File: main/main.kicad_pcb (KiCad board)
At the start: 2 copper layers, 100 x 100 mm, 251 parts, among them J1 USB_C_Receptacle, J2 SWD, Q1 BSS138, SW1 SW_SPST, SW2 SW_SPST, SW3 SW_SPST, SW4 SW_SPST, SW5 SW_SPST, SW6 SW_SPST, U1 LN6206P332MR-G, U2 STM32F401CBUx, Y1 Crystal

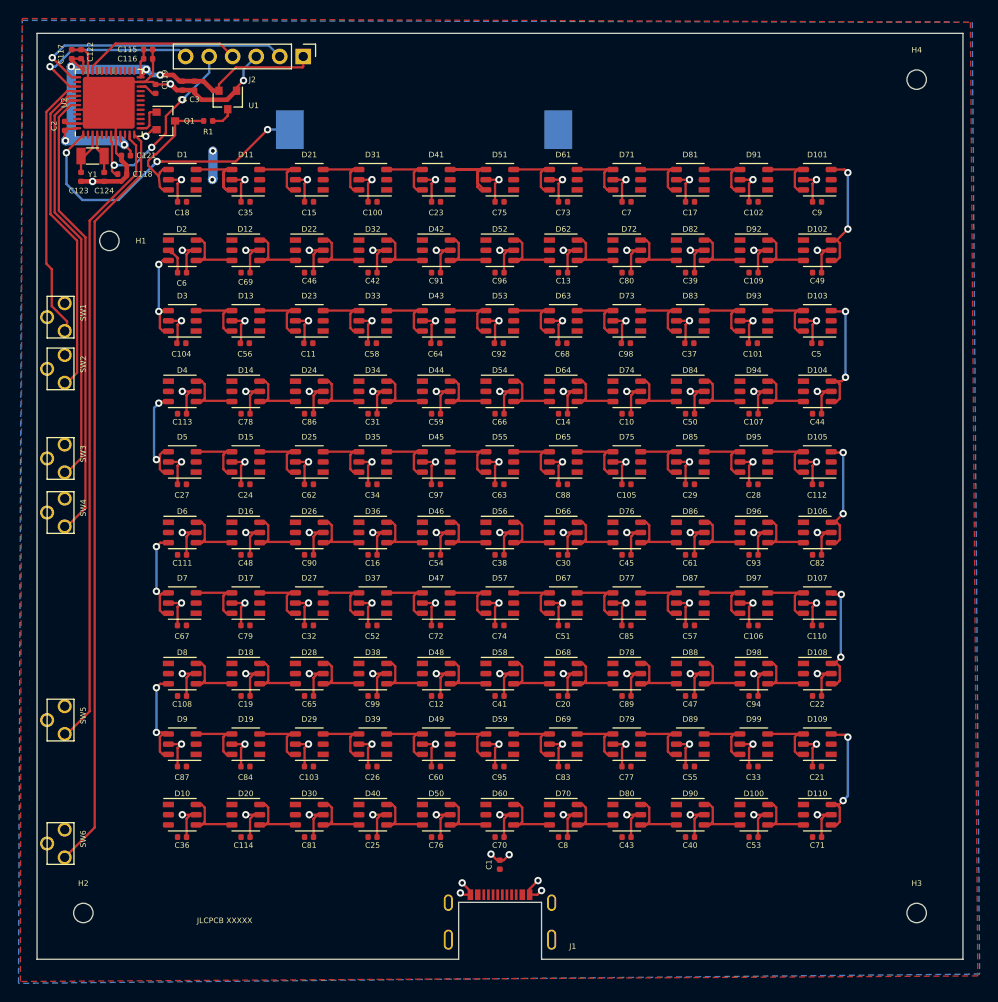
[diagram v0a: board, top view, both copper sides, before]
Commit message: made spacer layer, replaces Ws2813 with WS2812, fixed fabrication for v0.0.0, now v0.1.0
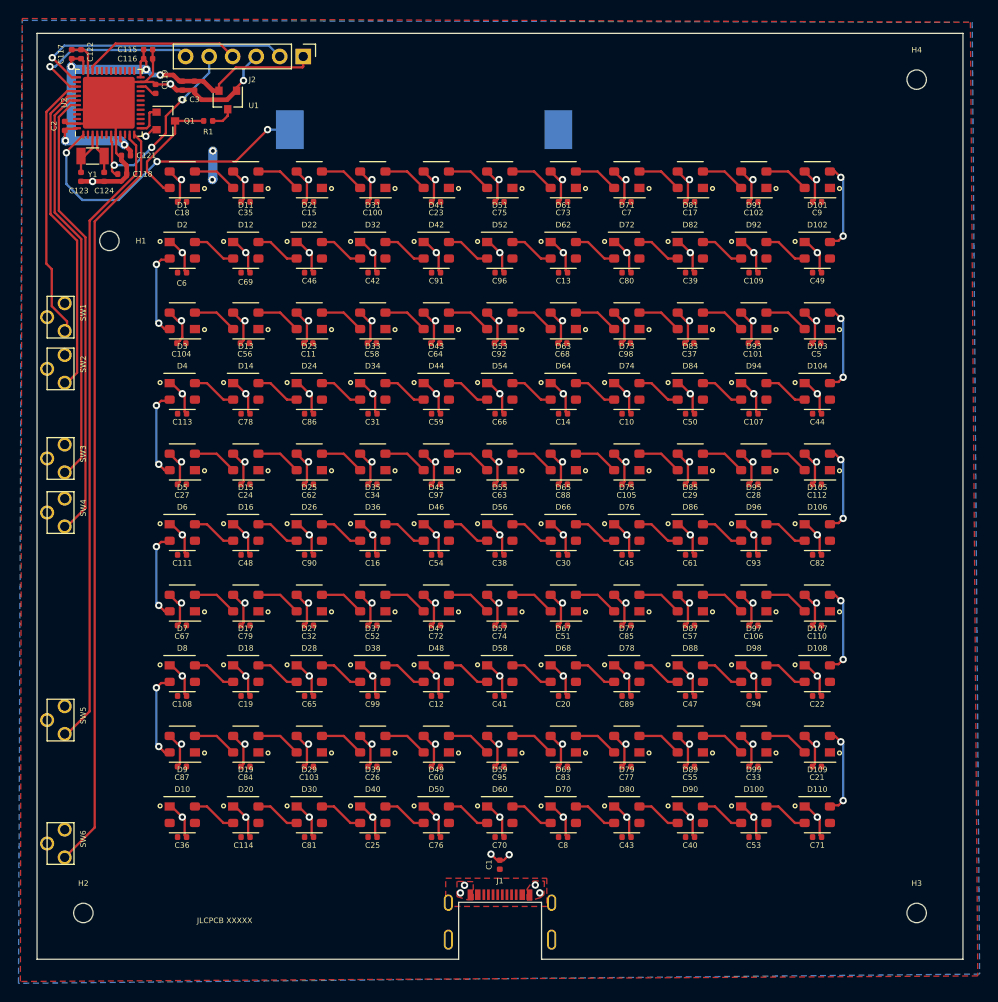
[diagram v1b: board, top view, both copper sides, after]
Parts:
- C118: value 10N -> 100N
- C119: value 2U2 -> 4U7
- C123, C124: value 21P -> 20P
- C4: value 10U -> 4U7
- D1, D10, D100, D101, D102, D103, D104, D105, D106, D107, D108, D109, D11, D110, D12, D13, D14, D15, D16, D17, D18, D19, D2, D20, D21, D22, D23, D24, D25, D26, D27, D28, D29, D3, D30, D31, D32, D33, D34, D35, D36, D37, D38, D39, D4, D40, D41, D42, D43, D44, D45, D46, D47, D48, D49, D5, D50, D51, D52, D53, D54, D55, D56, D57, D58, D59, D6, D60, D61, D62, D63, D64, D65, D66, D67, D68, D69, D7, D70, D71, D72, D73, D74, D75, D76, D77, D78, D79, D8, D80, D81, D82, D83, D84, D85, D86, D87, D88, D89, D9, D90, D91, D92, D93, D94, D95, D96, D97, D98, D99: value WS2813-Mini -> WS2812B-MINI; footprint william_led:WS2813-Mini-3.5mm_x_3.5mm -> william_led:WS2812B_v3-MINI
- J1: value USB_C_Receptacle -> USB_C_Receptacle_USB2.0
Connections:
- D1 pad 2: +5V -> Net-(D1-Pad2)
- D1 pad 3: Net-(D1-Pad3) -> GND
- D10 pad 1: +5V -> GND
- D10 pad 2: +5V -> /LEDs/DOUT
- D10 pad 3: (no net) -> +5V
- D100 pad 1: +5V -> GND
- D100 pad 2: +5V -> Net-(D100-Pad2)
- D100 pad 3: Net-(D100-Pad3) -> +5V
- D101 pad 2: +5V -> Net-(D101-Pad2)
- D101 pad 3: Net-(D101-Pad3) -> GND
- D102 pad 1: +5V -> GND
- D102 pad 2: +5V -> Net-(D102-Pad2)
- D102 pad 3: Net-(D102-Pad3) -> +5V
- D102 pad 4: Net-(D101-Pad3) -> Net-(D101-Pad2)
- D103 pad 2: +5V -> Net-(D103-Pad2)
- D103 pad 3: Net-(D103-Pad3) -> GND
- D104 pad 1: +5V -> GND
- D104 pad 2: +5V -> Net-(D104-Pad2)
- D104 pad 3: Net-(D104-Pad3) -> +5V
- D104 pad 4: Net-(D103-Pad3) -> Net-(D103-Pad2)
- D105 pad 2: +5V -> Net-(D105-Pad2)
- D105 pad 3: Net-(D105-Pad3) -> GND
- D106 pad 1: +5V -> GND
- D106 pad 2: +5V -> Net-(D106-Pad2)
- D106 pad 3: Net-(D106-Pad3) -> +5V
- D106 pad 4: Net-(D105-Pad3) -> Net-(D105-Pad2)
- D107 pad 2: +5V -> Net-(D107-Pad2)
- D107 pad 3: Net-(D107-Pad3) -> GND
- D108 pad 1: +5V -> GND
- D108 pad 2: +5V -> Net-(D108-Pad2)
- D108 pad 3: Net-(D108-Pad3) -> +5V
- D108 pad 4: Net-(D107-Pad3) -> Net-(D107-Pad2)
- D109 pad 2: +5V -> Net-(D109-Pad2)
- D109 pad 3: Net-(D109-Pad3) -> GND
- D11 pad 2: +5V -> Net-(D11-Pad2)
- D11 pad 3: Net-(D11-Pad3) -> GND
- D11 pad 4: Net-(D1-Pad3) -> Net-(D1-Pad2)
- D110 pad 1: +5V -> GND
- D110 pad 2: +5V -> Net-(D100-Pad4)
- D110 pad 3: Net-(D100-Pad4) -> +5V
- D110 pad 4: Net-(D109-Pad3) -> Net-(D109-Pad2)
- D12 pad 1: +5V -> GND
- D12 pad 2: +5V -> Net-(D12-Pad2)
- D12 pad 3: Net-(D12-Pad3) -> +5V
- D13 pad 2: +5V -> Net-(D13-Pad2)
- D13 pad 3: Net-(D13-Pad3) -> GND
- D14 pad 1: +5V -> GND
- D14 pad 2: +5V -> Net-(D14-Pad2)
- D14 pad 3: Net-(D14-Pad3) -> +5V
- D15 pad 2: +5V -> Net-(D15-Pad2)
- D15 pad 3: Net-(D15-Pad3) -> GND
- D16 pad 1: +5V -> GND
- D16 pad 2: +5V -> Net-(D16-Pad2)
- D16 pad 3: Net-(D16-Pad3) -> +5V
- D17 pad 2: +5V -> Net-(D17-Pad2)
- D17 pad 3: Net-(D17-Pad3) -> GND
- D18 pad 1: +5V -> GND
- D18 pad 2: +5V -> Net-(D18-Pad2)
- D18 pad 3: Net-(D18-Pad3) -> +5V
- D19 pad 2: +5V -> Net-(D19-Pad2)
- D19 pad 3: Net-(D19-Pad3) -> GND
- D2 pad 1: +5V -> GND
- D2 pad 2: +5V -> Net-(D2-Pad2)
- D2 pad 3: Net-(D2-Pad3) -> +5V
- D2 pad 4: Net-(D12-Pad3) -> Net-(D12-Pad2)
- D20 pad 1: +5V -> GND
- D20 pad 2: +5V -> Net-(D10-Pad4)
- D20 pad 3: Net-(D10-Pad4) -> +5V
- D21 pad 2: +5V -> Net-(D21-Pad2)
- D21 pad 3: Net-(D21-Pad3) -> GND
- D21 pad 4: Net-(D11-Pad3) -> Net-(D11-Pad2)
- D22 pad 1: +5V -> GND
- D22 pad 2: +5V -> Net-(D12-Pad4)
- D22 pad 3: Net-(D12-Pad4) -> +5V
- D23 pad 2: +5V -> Net-(D23-Pad2)
- D23 pad 3: Net-(D23-Pad3) -> GND
- D23 pad 4: Net-(D13-Pad3) -> Net-(D13-Pad2)
- D24 pad 1: +5V -> GND
- D24 pad 2: +5V -> Net-(D14-Pad4)
- D24 pad 3: Net-(D14-Pad4) -> +5V
- D25 pad 2: +5V -> Net-(D25-Pad2)
- D25 pad 3: Net-(D25-Pad3) -> GND
- D25 pad 4: Net-(D15-Pad3) -> Net-(D15-Pad2)
- D26 pad 1: +5V -> GND
- D26 pad 2: +5V -> Net-(D16-Pad4)
- D26 pad 3: Net-(D16-Pad4) -> +5V
- D27 pad 2: +5V -> Net-(D27-Pad2)
- D27 pad 3: Net-(D27-Pad3) -> GND
- D27 pad 4: Net-(D17-Pad3) -> Net-(D17-Pad2)
- D28 pad 1: +5V -> GND
- D28 pad 2: +5V -> Net-(D18-Pad4)
- D28 pad 3: Net-(D18-Pad4) -> +5V
- D29 pad 2: +5V -> Net-(D29-Pad2)
- D29 pad 3: Net-(D29-Pad3) -> GND
- D29 pad 4: Net-(D19-Pad3) -> Net-(D19-Pad2)
- D3 pad 2: +5V -> Net-(D13-Pad4)
- D3 pad 3: Net-(D13-Pad4) -> GND
- D3 pad 4: Net-(D2-Pad3) -> Net-(D2-Pad2)
- D30 pad 1: +5V -> GND
- D30 pad 2: +5V -> Net-(D20-Pad4)
- D30 pad 3: Net-(D20-Pad4) -> +5V
- D31 pad 2: +5V -> Net-(D31-Pad2)
- D31 pad 3: Net-(D31-Pad3) -> GND
- D31 pad 4: Net-(D21-Pad3) -> Net-(D21-Pad2)
- D32 pad 1: +5V -> GND
- D32 pad 2: +5V -> Net-(D22-Pad4)
- D32 pad 3: Net-(D22-Pad4) -> +5V
- D33 pad 2: +5V -> Net-(D33-Pad2)
- D33 pad 3: Net-(D33-Pad3) -> GND
- D33 pad 4: Net-(D23-Pad3) -> Net-(D23-Pad2)
- D34 pad 1: +5V -> GND
- D34 pad 2: +5V -> Net-(D24-Pad4)
- D34 pad 3: Net-(D24-Pad4) -> +5V
- D35 pad 2: +5V -> Net-(D35-Pad2)
- D35 pad 3: Net-(D35-Pad3) -> GND
- D35 pad 4: Net-(D25-Pad3) -> Net-(D25-Pad2)
- D36 pad 1: +5V -> GND
- D36 pad 2: +5V -> Net-(D26-Pad4)
- D36 pad 3: Net-(D26-Pad4) -> +5V
- D37 pad 2: +5V -> Net-(D37-Pad2)
- D37 pad 3: Net-(D37-Pad3) -> GND
- D37 pad 4: Net-(D27-Pad3) -> Net-(D27-Pad2)
- D38 pad 1: +5V -> GND
- D38 pad 2: +5V -> Net-(D28-Pad4)
- D38 pad 3: Net-(D28-Pad4) -> +5V
- D39 pad 2: +5V -> Net-(D39-Pad2)
- D39 pad 3: Net-(D39-Pad3) -> GND
- D39 pad 4: Net-(D29-Pad3) -> Net-(D29-Pad2)
- D4 pad 1: +5V -> GND
- D4 pad 2: +5V -> Net-(D4-Pad2)
- D4 pad 3: Net-(D4-Pad3) -> +5V
- D4 pad 4: Net-(D14-Pad3) -> Net-(D14-Pad2)
- D40 pad 1: +5V -> GND
- D40 pad 2: +5V -> Net-(D30-Pad4)
- D40 pad 3: Net-(D30-Pad4) -> +5V
- D41 pad 2: +5V -> Net-(D41-Pad2)
- D41 pad 3: Net-(D41-Pad3) -> GND
- D41 pad 4: Net-(D31-Pad3) -> Net-(D31-Pad2)
- D42 pad 1: +5V -> GND
- D42 pad 2: +5V -> Net-(D32-Pad4)
- D42 pad 3: Net-(D32-Pad4) -> +5V
- D43 pad 2: +5V -> Net-(D43-Pad2)
- D43 pad 3: Net-(D43-Pad3) -> GND
- D43 pad 4: Net-(D33-Pad3) -> Net-(D33-Pad2)
- D44 pad 1: +5V -> GND
- D44 pad 2: +5V -> Net-(D34-Pad4)
- D44 pad 3: Net-(D34-Pad4) -> +5V
- D45 pad 2: +5V -> Net-(D45-Pad2)
- D45 pad 3: Net-(D45-Pad3) -> GND
- D45 pad 4: Net-(D35-Pad3) -> Net-(D35-Pad2)
- D46 pad 1: +5V -> GND
- D46 pad 2: +5V -> Net-(D36-Pad4)
- D46 pad 3: Net-(D36-Pad4) -> +5V
- D47 pad 2: +5V -> Net-(D47-Pad2)
- D47 pad 3: Net-(D47-Pad3) -> GND
- D47 pad 4: Net-(D37-Pad3) -> Net-(D37-Pad2)
- D48 pad 1: +5V -> GND
- D48 pad 2: +5V -> Net-(D38-Pad4)
- D48 pad 3: Net-(D38-Pad4) -> +5V
- D49 pad 2: +5V -> Net-(D49-Pad2)
- D49 pad 3: Net-(D49-Pad3) -> GND
- D49 pad 4: Net-(D39-Pad3) -> Net-(D39-Pad2)
- D5 pad 2: +5V -> Net-(D15-Pad4)
- D5 pad 3: Net-(D15-Pad4) -> GND
- D5 pad 4: Net-(D4-Pad3) -> Net-(D4-Pad2)
- D50 pad 1: +5V -> GND
- D50 pad 2: +5V -> Net-(D40-Pad4)
- D50 pad 3: Net-(D40-Pad4) -> +5V
- D51 pad 2: +5V -> Net-(D51-Pad2)
- D51 pad 3: Net-(D51-Pad3) -> GND
- D51 pad 4: Net-(D41-Pad3) -> Net-(D41-Pad2)
- D52 pad 1: +5V -> GND
- D52 pad 2: +5V -> Net-(D42-Pad4)
- D52 pad 3: Net-(D42-Pad4) -> +5V
- D53 pad 2: +5V -> Net-(D53-Pad2)
- D53 pad 3: Net-(D53-Pad3) -> GND
- D53 pad 4: Net-(D43-Pad3) -> Net-(D43-Pad2)
- D54 pad 1: +5V -> GND
- D54 pad 2: +5V -> Net-(D44-Pad4)
- D54 pad 3: Net-(D44-Pad4) -> +5V
- D55 pad 2: +5V -> Net-(D55-Pad2)
- D55 pad 3: Net-(D55-Pad3) -> GND
- D55 pad 4: Net-(D45-Pad3) -> Net-(D45-Pad2)
- D56 pad 1: +5V -> GND
- D56 pad 2: +5V -> Net-(D46-Pad4)
- D56 pad 3: Net-(D46-Pad4) -> +5V
- D57 pad 2: +5V -> Net-(D57-Pad2)
- D57 pad 3: Net-(D57-Pad3) -> GND
- D57 pad 4: Net-(D47-Pad3) -> Net-(D47-Pad2)
- D58 pad 1: +5V -> GND
- D58 pad 2: +5V -> Net-(D48-Pad4)
- D58 pad 3: Net-(D48-Pad4) -> +5V
- D59 pad 2: +5V -> Net-(D59-Pad2)
- D59 pad 3: Net-(D59-Pad3) -> GND
- D59 pad 4: Net-(D49-Pad3) -> Net-(D49-Pad2)
- D6 pad 1: +5V -> GND
- D6 pad 2: +5V -> Net-(D6-Pad2)
- D6 pad 3: Net-(D6-Pad3) -> +5V
- D6 pad 4: Net-(D16-Pad3) -> Net-(D16-Pad2)
- D60 pad 1: +5V -> GND
- D60 pad 2: +5V -> Net-(D50-Pad4)
- D60 pad 3: Net-(D50-Pad4) -> +5V
- D61 pad 2: +5V -> Net-(D61-Pad2)
- D61 pad 3: Net-(D61-Pad3) -> GND
- D61 pad 4: Net-(D51-Pad3) -> Net-(D51-Pad2)
- D62 pad 1: +5V -> GND
- D62 pad 2: +5V -> Net-(D52-Pad4)
- D62 pad 3: Net-(D52-Pad4) -> +5V
- D63 pad 2: +5V -> Net-(D63-Pad2)
- D63 pad 3: Net-(D63-Pad3) -> GND
- D63 pad 4: Net-(D53-Pad3) -> Net-(D53-Pad2)
- D64 pad 1: +5V -> GND
- D64 pad 2: +5V -> Net-(D54-Pad4)
- D64 pad 3: Net-(D54-Pad4) -> +5V
- D65 pad 2: +5V -> Net-(D65-Pad2)
- D65 pad 3: Net-(D65-Pad3) -> GND
- D65 pad 4: Net-(D55-Pad3) -> Net-(D55-Pad2)
- D66 pad 1: +5V -> GND
- D66 pad 2: +5V -> Net-(D56-Pad4)
- D66 pad 3: Net-(D56-Pad4) -> +5V
- D67 pad 2: +5V -> Net-(D67-Pad2)
- D67 pad 3: Net-(D67-Pad3) -> GND
- D67 pad 4: Net-(D57-Pad3) -> Net-(D57-Pad2)
- D68 pad 1: +5V -> GND
- D68 pad 2: +5V -> Net-(D58-Pad4)
- D68 pad 3: Net-(D58-Pad4) -> +5V
- D69 pad 2: +5V -> Net-(D69-Pad2)
- D69 pad 3: Net-(D69-Pad3) -> GND
- D69 pad 4: Net-(D59-Pad3) -> Net-(D59-Pad2)
- D7 pad 2: +5V -> Net-(D17-Pad4)
- D7 pad 3: Net-(D17-Pad4) -> GND
- D7 pad 4: Net-(D6-Pad3) -> Net-(D6-Pad2)
- D70 pad 1: +5V -> GND
- D70 pad 2: +5V -> Net-(D60-Pad4)
- D70 pad 3: Net-(D60-Pad4) -> +5V
- D71 pad 2: +5V -> Net-(D71-Pad2)
- D71 pad 3: Net-(D71-Pad3) -> GND
- D71 pad 4: Net-(D61-Pad3) -> Net-(D61-Pad2)
- D72 pad 1: +5V -> GND
- D72 pad 2: +5V -> Net-(D62-Pad4)
- D72 pad 3: Net-(D62-Pad4) -> +5V
- D73 pad 2: +5V -> Net-(D73-Pad2)
- D73 pad 3: Net-(D73-Pad3) -> GND
- D73 pad 4: Net-(D63-Pad3) -> Net-(D63-Pad2)
- D74 pad 1: +5V -> GND
- D74 pad 2: +5V -> Net-(D64-Pad4)
- D74 pad 3: Net-(D64-Pad4) -> +5V
- D75 pad 2: +5V -> Net-(D75-Pad2)
- D75 pad 3: Net-(D75-Pad3) -> GND
- D75 pad 4: Net-(D65-Pad3) -> Net-(D65-Pad2)
- D76 pad 1: +5V -> GND
- D76 pad 2: +5V -> Net-(D66-Pad4)
- D76 pad 3: Net-(D66-Pad4) -> +5V
- D77 pad 2: +5V -> Net-(D77-Pad2)
- D77 pad 3: Net-(D77-Pad3) -> GND
- D77 pad 4: Net-(D67-Pad3) -> Net-(D67-Pad2)
- D78 pad 1: +5V -> GND
- D78 pad 2: +5V -> Net-(D68-Pad4)
- D78 pad 3: Net-(D68-Pad4) -> +5V
- D79 pad 2: +5V -> Net-(D79-Pad2)
- D79 pad 3: Net-(D79-Pad3) -> GND
- D79 pad 4: Net-(D69-Pad3) -> Net-(D69-Pad2)
- D8 pad 1: +5V -> GND
- D8 pad 2: +5V -> Net-(D8-Pad2)
- D8 pad 3: Net-(D8-Pad3) -> +5V
- D8 pad 4: Net-(D18-Pad3) -> Net-(D18-Pad2)
- D80 pad 1: +5V -> GND
- D80 pad 2: +5V -> Net-(D70-Pad4)
- D80 pad 3: Net-(D70-Pad4) -> +5V
- D81 pad 2: +5V -> Net-(D81-Pad2)
- D81 pad 3: Net-(D81-Pad3) -> GND
- D81 pad 4: Net-(D71-Pad3) -> Net-(D71-Pad2)
- D82 pad 1: +5V -> GND
- D82 pad 2: +5V -> Net-(D72-Pad4)
- D82 pad 3: Net-(D72-Pad4) -> +5V
- D83 pad 2: +5V -> Net-(D83-Pad2)
- D83 pad 3: Net-(D83-Pad3) -> GND
- D83 pad 4: Net-(D73-Pad3) -> Net-(D73-Pad2)
- D84 pad 1: +5V -> GND
- D84 pad 2: +5V -> Net-(D74-Pad4)
- D84 pad 3: Net-(D74-Pad4) -> +5V
- D85 pad 2: +5V -> Net-(D85-Pad2)
- D85 pad 3: Net-(D85-Pad3) -> GND
- D85 pad 4: Net-(D75-Pad3) -> Net-(D75-Pad2)
- D86 pad 1: +5V -> GND
- D86 pad 2: +5V -> Net-(D76-Pad4)
- D86 pad 3: Net-(D76-Pad4) -> +5V
- D87 pad 2: +5V -> Net-(D87-Pad2)
- D87 pad 3: Net-(D87-Pad3) -> GND
- D87 pad 4: Net-(D77-Pad3) -> Net-(D77-Pad2)
- D88 pad 1: +5V -> GND
- D88 pad 2: +5V -> Net-(D78-Pad4)
- D88 pad 3: Net-(D78-Pad4) -> +5V
- D89 pad 2: +5V -> Net-(D89-Pad2)
- D89 pad 3: Net-(D89-Pad3) -> GND
- D89 pad 4: Net-(D79-Pad3) -> Net-(D79-Pad2)
- D9 pad 2: +5V -> Net-(D19-Pad4)
- D9 pad 3: Net-(D19-Pad4) -> GND
- D9 pad 4: Net-(D8-Pad3) -> Net-(D8-Pad2)
- D90 pad 1: +5V -> GND
- D90 pad 2: +5V -> Net-(D80-Pad4)
- D90 pad 3: Net-(D80-Pad4) -> +5V
- D90 pad 4: Net-(D100-Pad3) -> Net-(D100-Pad2)
- D91 pad 2: +5V -> Net-(D101-Pad4)
- D91 pad 3: Net-(D101-Pad4) -> GND
- D91 pad 4: Net-(D81-Pad3) -> Net-(D81-Pad2)
- D92 pad 1: +5V -> GND
- D92 pad 2: +5V -> Net-(D82-Pad4)
- D92 pad 3: Net-(D82-Pad4) -> +5V
- D92 pad 4: Net-(D102-Pad3) -> Net-(D102-Pad2)
- D93 pad 2: +5V -> Net-(D103-Pad4)
- D93 pad 3: Net-(D103-Pad4) -> GND
- D93 pad 4: Net-(D83-Pad3) -> Net-(D83-Pad2)
- D94 pad 1: +5V -> GND
- D94 pad 2: +5V -> Net-(D84-Pad4)
- D94 pad 3: Net-(D84-Pad4) -> +5V
- D94 pad 4: Net-(D104-Pad3) -> Net-(D104-Pad2)
- D95 pad 2: +5V -> Net-(D105-Pad4)
- D95 pad 3: Net-(D105-Pad4) -> GND
- D95 pad 4: Net-(D85-Pad3) -> Net-(D85-Pad2)
- D96 pad 1: +5V -> GND
- D96 pad 2: +5V -> Net-(D86-Pad4)
- D96 pad 3: Net-(D86-Pad4) -> +5V
- D96 pad 4: Net-(D106-Pad3) -> Net-(D106-Pad2)
- D97 pad 2: +5V -> Net-(D107-Pad4)
- D97 pad 3: Net-(D107-Pad4) -> GND
- D97 pad 4: Net-(D87-Pad3) -> Net-(D87-Pad2)
- D98 pad 1: +5V -> GND
- D98 pad 2: +5V -> Net-(D88-Pad4)
- D98 pad 3: Net-(D88-Pad4) -> +5V
- D98 pad 4: Net-(D108-Pad3) -> Net-(D108-Pad2)
- D99 pad 2: +5V -> Net-(D109-Pad4)
- D99 pad 3: Net-(D109-Pad4) -> GND
- D99 pad 4: Net-(D89-Pad3) -> Net-(D89-Pad2)
- J1 pad A5: (no net) -> Net-(J1-PadA5)
- J1 pad A6: (no net) -> Net-(J1-PadA6)
- J1 pad A7: (no net) -> Net-(J1-PadA7)
- J1 pad A8: (no net) -> Net-(J1-PadA8)
- J1 pad B5: (no net) -> Net-(J1-PadB5)
- J1 pad B6: (no net) -> Net-(J1-PadB6)
- J1 pad B7: (no net) -> Net-(J1-PadB7)
- J1 pad B8: (no net) -> Net-(J1-PadB8)
- U2 pad 10: (no net) -> Net-(U2-Pad10)
- U2 pad 14: (no net) -> Net-(U2-Pad14)
- U2 pad 15: (no net) -> Net-(U2-Pad15)
- U2 pad 16: (no net) -> Net-(U2-Pad16)
- U2 pad 17: (no net) -> Net-(U2-Pad17)
- U2 pad 18: (no net) -> Net-(U2-Pad18)
- U2 pad 19: (no net) -> Net-(U2-Pad19)
- U2 pad 2: (no net) -> Net-(U2-Pad2)
- U2 pad 20: (no net) -> Net-(U2-Pad20)
- U2 pad 21: (no net) -> Net-(U2-Pad21)
- U2 pad 25: (no net) -> Net-(U2-Pad25)
- U2 pad 26: (no net) -> Net-(U2-Pad26)
- U2 pad 27: (no net) -> Net-(U2-Pad27)
- U2 pad 28: (no net) -> Net-(U2-Pad28)
- U2 pad 29: (no net) -> Net-(U2-Pad29)
- U2 pad 30: (no net) -> Net-(U2-Pad30)
- U2 pad 31: (no net) -> Net-(U2-Pad31)
- U2 pad 32: (no net) -> Net-(U2-Pad32)
- U2 pad 33: (no net) -> Net-(U2-Pad33)
- U2 pad 38: (no net) -> Net-(U2-Pad38)
- U2 pad 45: (no net) -> Net-(U2-Pad45)
- U2 pad 46: (no net) -> Net-(U2-Pad46)
- U2 pad 5: (no net) -> Net-(U2-Pad5)
- U2 pad 6: (no net) -> Net-(U2-Pad6)
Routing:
- net GND: track 544.6 -> 523.4 mm
- net Net-(D41-Pad3): track 14.8 -> 0.00 mm
- net Net-(D109-Pad3): track 14.1 -> 0.00 mm, vias 2 -> 0
- net Net-(D103-Pad3): track 14.1 -> 0.00 mm, vias 2 -> 0
- net Net-(D101-Pad3): track 13.4 -> 0.00 mm, vias 2 -> 0
- net Net-(D105-Pad3): track 13.3 -> 0.00 mm, vias 2 -> 0
- net Net-(D107-Pad3): track 13.0 -> 0.00 mm, vias 2 -> 0
- net Net-(D4-Pad3): track 11.6 -> 0.00 mm, vias 2 -> 0
- net Net-(D6-Pad3): track 11.4 -> 0.00 mm, vias 2 -> 0
- net Net-(D8-Pad3): track 11.3 -> 0.00 mm, vias 2 -> 0
- net Net-(D1-Pad3): track 11.2 -> 0.00 mm
- net Net-(D2-Pad3): track 11.0 -> 0.00 mm, vias 2 -> 0
- net Net-(D109-Pad2): track 0.00 -> 9.59 mm, vias 0 -> 2
- net Net-(D107-Pad2): track 0.00 -> 9.59 mm, vias 0 -> 2
- net Net-(D105-Pad2): track 0.00 -> 9.59 mm, vias 0 -> 2
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- added copper zone on F.Cu, net GND
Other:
- board text added: "WORD CLOCK v0.1.0 batch 0 12/11/2019"
- board text removed: "WORD CLOCK v0.0.0 batch 0 12/11/2019"

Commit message: added 4 more leds for minute-specific indicator
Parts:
- added C120: 100N, Capacitor_SMD:C_0402_1005Metric, F.Cu at (19.2, 96.0)
- added C125: 100N, Capacitor_SMD:C_0402_1005Metric, F.Cu at (31.4, 96.2)
- added C126: 100N, Capacitor_SMD:C_0402_1005Metric, F.Cu at (68.8, 97.0)
- added C127: 100N, Capacitor_SMD:C_0402_1005Metric, F.Cu at (81.1, 96.3)
- added D111: WS2812B-MINI, william_led:WS2812B_v3-MINI, F.Cu at (18.9, 92.4)
- added D112: WS2812B-MINI, william_led:WS2812B_v3-MINI, F.Cu at (31.2, 92.4)
- added D113: WS2812B-MINI, william_led:WS2812B_v3-MINI, F.Cu at (68.8, 92.4)
- added D114: WS2812B-MINI, william_led:WS2812B_v3-MINI, F.Cu at (81.1, 92.4)
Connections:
- D10 pad 2: /LEDs/DOUT -> Net-(D10-Pad2)
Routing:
- net Net-(D112-Pad2): track 0.00 -> 37.9 mm, vias 0 -> 6
- net GND: track 523.4 -> 542.2 mm, vias 120 -> 124
- net Net-(D10-Pad2): track 0.00 -> 11.7 mm, vias 0 -> 2
- net Net-(D113-Pad2): track 0.00 -> 10.3 mm, vias 0 -> 2
- net Net-(D111-Pad2): track 0.00 -> 10.2 mm, vias 0 -> 2

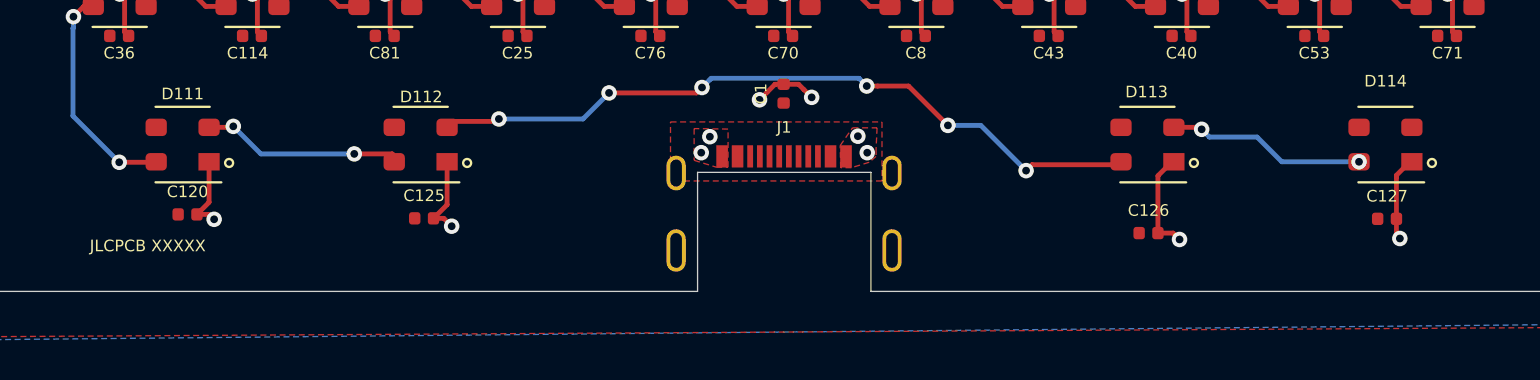
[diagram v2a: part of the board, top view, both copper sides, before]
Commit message: moved caps in to LEDs so they'd fit under hole
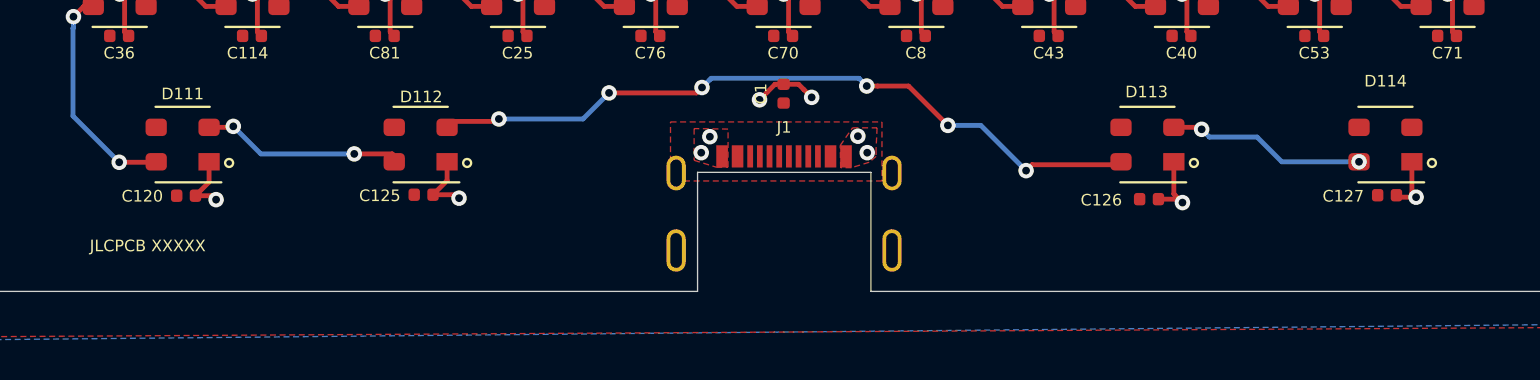
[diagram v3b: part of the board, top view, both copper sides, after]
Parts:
- moved C126 1.75 mm to (68.9, 95.2)
- moved C125 1.22 mm to (31.4, 95.0)
- moved C127 1.22 mm to (81.1, 95.0)
- moved C120 0.97 mm to (19.1, 95.1)
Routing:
- net GND: track 542.2 -> 537.4 mm
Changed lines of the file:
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@@
     (thickness 1.6)
     (drawings 20)
-    (tracks 1301)
+    (tracks 1298)
     (zones 0)
     (modules 259)
@@
   )
   (module Capacitor_SMD:C_0402_1005Metric (layer F.Cu)
-    (at 81.1438 96.2518)
+    (at 81.1438 95.0326)
     (descr "Capacitor SMD 0402 (1005 Metric), square (rectangular) end terminal, IPC_7351 nominal, (Body size source: http://www.tortai-tech.com/upload/download/2011102023233369053.pdf), generated with kicad-footprint-generator")
     (tags capacitor)
     (attr smd)
-    (fp_text reference C127 (at 0 -1.17) (layer F.SilkS)
+    (fp_text reference C127 (at -2.2606 0.0508) (layer F.SilkS)
       (effects (font (size 0.6 0.6) (thickness 0.13)))
     )
@@
   )
   (module Capacitor_SMD:C_0402_1005Metric (layer F.Cu)
-    (at 68.8248 96.9884)
+    (at 68.8502 95.2358)
     (descr "Capacitor SMD 0402 (1005 Metric), square (rectangular) end terminal, IPC_7351 nominal, (Body size source: http://www.tortai-tech.com/upload/download/2011102023233369053.pdf), generated with kicad-footprint-generator")
     (tags capacitor)
     (attr smd)
-    (fp_text reference C126 (at 0 -1.17) (layer F.SilkS)
+    (fp_text reference C126 (at -2.4638 0.0508) (layer F.SilkS)
       (effects (font (size 0.6 0.6) (thickness 0.13)))
     )
@@
   )
   (module Capacitor_SMD:C_0402_1005Metric (layer F.Cu)
-    (at 31.4106 96.2264)
+    (at 31.3852 95.0072)
     (descr "Capacitor SMD 0402 (1005 Metric), square (rectangular) end terminal, IPC_7351 nominal, (Body size source: http://www.tortai-tech.com/upload/download/2011102023233369053.pdf), generated with kicad-footprint-generator")
     (tags capacitor)
     (attr smd)
-    (fp_text reference C125 (at 0 -1.17) (layer F.SilkS)
+    (fp_text reference C125 (at -2.2606 0.0508) (layer F.SilkS)
       (effects (font (size 0.6 0.6) (thickness 0.13)))
     )
@@
   )
   (module Capacitor_SMD:C_0402_1005Metric (layer F.Cu)
-    (at 19.1932 96.0232)
+    (at 19.117 95.058)
     (descr "Capacitor SMD 0402 (1005 Metric), square (rectangular) end terminal, IPC_7351 nominal, (Body size source: http://www.tortai-tech.com/upload/download/2011102023233369053.pdf), generated with kicad-footprint-generator")
     (tags capacitor)
     (attr smd)
-    (fp_text reference C120 (at 0 -1.17) (layer F.SilkS)
+    (fp_text reference C120 (at -2.2606 0.0254) (layer F.SilkS)
       (effects (font (size 0.6 0.6) (thickness 0.13)))
     )
@@
   (via (at 53.8134 91.9846) (size 0.8) (drill 0.4) (layers F.Cu B.Cu) (net 1))
   (via (at 46.168 92.01) (size 0.8) (drill 0.4) (layers F.Cu B.Cu) (net 1))
-  (segment (start 82.3258 93.3064) (end 82.4258 93.3064) (width 0.25) (layer F.Cu) (net 1))
-  (segment (start 81.6258 94.0064) (end 82.3258 93.3064) (width 0.25) (layer F.Cu) (net 1))
-  (segment (start 81.6258 94.1004) (end 81.6258 94.0064) (width 0.25) (layer F.Cu) (net 1))
-  (segment (start 81.6288 94.1034) (end 81.6258 94.1004) (width 0.25) (layer F.Cu) (net 1))
-  (segment (start 81.6288 96.2518) (end 81.6288 94.1034) (width 0.25) (layer F.Cu) (net 1))
-  (via (at 81.8042 97.2678) (size 0.8) (drill 0.4) (layers F.Cu B.Cu) (net 1))
-  (segment (start 81.6288 96.2518) (end 81.6288 97.0924) (width 0.25) (layer F.Cu) (net 1))
-  (segment (start 81.6288 97.0924) (end 81.8042 97.2678) (width 0.25) (layer F.Cu) (net 1))
-  (segment (start 70.0322 93.3064) (end 70.1322 93.3064) (width 0.25) (layer F.Cu) (net 1))
-  (segment (start 69.3098 94.0288) (end 70.0322 93.3064) (width 0.25) (layer F.Cu) (net 1))
-  (segment (start 69.3098 96.9884) (end 69.3098 94.0288) (width 0.25) (layer F.Cu) (net 1))
-  (via (at 70.425 97.3186) (size 0.8) (drill 0.4) (layers F.Cu B.Cu) (net 1))
-  (segment (start 69.3098 96.9884) (end 70.0948 96.9884) (width 0.25) (layer F.Cu) (net 1))
-  (segment (start 70.0948 96.9884) (end 70.425 97.3186) (width 0.25) (layer F.Cu) (net 1))
-  (segment (start 32.5978 95.5242) (end 32.5978 93.3064) (width 0.25) (layer F.Cu) (net 1))
-  (segment (start 31.8956 96.2264) (end 32.5978 95.5242) (width 0.25) (layer F.Cu) (net 1))
-  (via (at 32.833 96.6328) (size 0.8) (drill 0.4) (layers F.Cu B.Cu) (net 1))
-  (segment (start 31.8956 96.2264) (end 32.4266 96.2264) (width 0.25) (layer F.Cu) (net 1))
-  (segment (start 32.4266 96.2264) (end 32.833 96.6328) (width 0.25) (layer F.Cu) (net 1))
-  (segment (start 20.3042 95.3972) (end 20.3042 93.3064) (width 0.25) (layer F.Cu) (net 1))
-  (segment (start 19.6782 96.0232) (end 20.3042 95.3972) (width 0.25) (layer F.Cu) (net 1))
-  (via (at 20.5648 96.2772) (size 0.8) (drill 0.4) (layers F.Cu B.Cu) (net 1))
-  (segment (start 19.6782 96.0232) (end 20.3108 96.0232) (width 0.25) (layer F.Cu) (net 1))
-  (segment (start 20.3108 96.0232) (end 20.5648 96.2772) (width 0.25) (layer F.Cu) (net 1))
   (segment (start 49.535896 89.3025) (end 49.133399 89.704997) (width 0.25) (layer F.Cu) (net 1))
   (segment (start 49.133399 89.704997) (end 48.7334 90.104996) (width 0.25) (layer F.Cu) (net 1))
@@
   (segment (start 51.025801 89.578001) (end 51.4258 89.978) (width 0.25) (layer F.Cu) (net 1))
   (segment (start 49.978 89.3025) (end 50.7503 89.3025) (width 0.25) (layer F.Cu) (net 1))
+  (segment (start 20.3042 94.3558) (end 20.3042 93.3064) (width 0.25) (layer F.Cu) (net 1))
+  (segment (start 19.602 95.058) (end 20.3042 94.3558) (width 0.25) (layer F.Cu) (net 1))
+  (via (at 20.6664 95.2612) (size 0.8) (drill 0.4) (layers F.Cu B.Cu) (net 1))
+  (segment (start 20.4632 95.058) (end 20.6664 95.2612) (width 0.25) (layer F.Cu) (net 1))
+  (segment (start 19.602 95.058) (end 20.4632 95.058) (width 0.25) (layer F.Cu) (net 1))
+  (segment (start 32.5978 94.2796) (end 32.5978 93.3064) (width 0.25) (layer F.Cu) (net 1))
+  (segment (start 31.8702 95.0072) (end 32.5978 94.2796) (width 0.25) (layer F.Cu) (net 1))
+  (via (at 33.214 95.185) (size 0.8) (drill 0.4) (layers F.Cu B.Cu) (net 1))
+  (segment (start 33.0362 95.0072) (end 33.214 95.185) (width 0.25) (layer F.Cu) (net 1))
+  (segment (start 31.8702 95.0072) (end 33.0362 95.0072) (width 0.25) (layer F.Cu) (net 1))
+  (via (at 70.5774 95.4136) (size 0.8) (drill 0.4) (layers F.Cu B.Cu) (net 1))
+  (segment (start 70.1322 93.3064) (end 70.1322 94.9684) (width 0.25) (layer F.Cu) (net 1))
+  (segment (start 70.177401 95.013601) (end 70.5774 95.4136) (width 0.25) (layer F.Cu) (net 1))
+  (segment (start 70.1322 94.9684) (end 70.177401 95.013601) (width 0.25) (layer F.Cu) (net 1))
+  (segment (start 70.3996 95.2358) (end 70.5774 95.4136) (width 0.25) (layer F.Cu) (net 1))
+  (segment (start 69.3352 95.2358) (end 70.3996 95.2358) (width 0.25) (layer F.Cu) (net 1))
+  (via (at 82.6424 95.1342) (size 0.8) (drill 0.4) (layers F.Cu B.Cu) (net 1))
+  (segment (start 82.4258 94.9176) (end 82.6424 95.1342) (width 0.25) (layer F.Cu) (net 1))
+  (segment (start 82.4258 93.3064) (end 82.4258 94.9176) (width 0.25) (layer F.Cu) (net 1))
+  (segment (start 81.7304 95.1342) (end 81.6288 95.0326) (width 0.25) (layer F.Cu) (net 1))
+  (segment (start 82.6424 95.1342) (end 81.7304 95.1342) (width 0.25) (layer F.Cu) (net 1))
   (segment (start 20.6 8.9) (end 20.6 8.2) (width 0.25) (layer F.Cu) (net 2) (status 20))
   (segment (start 20.04 9.46) (end 20.6 8.9) (width 0.25) (layer F.Cu) (net 2))
